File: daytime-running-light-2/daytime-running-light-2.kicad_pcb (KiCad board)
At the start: 2 copper layers, 163.2 x 88.6 mm, 58 parts, among them J1 Conn_01x01_Socket, J2 Conn_01x01_Socket, J3 Conn_01x01_Socket, J4 Conn_01x01_Socket, J5 Conn_01x01_Socket, J6 Conn_01x01_Pin, J7 Conn_01x01_Socket, J8 Conn_01x01_Socket, J9 Conn_01x01_Socket, Q1 BC548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

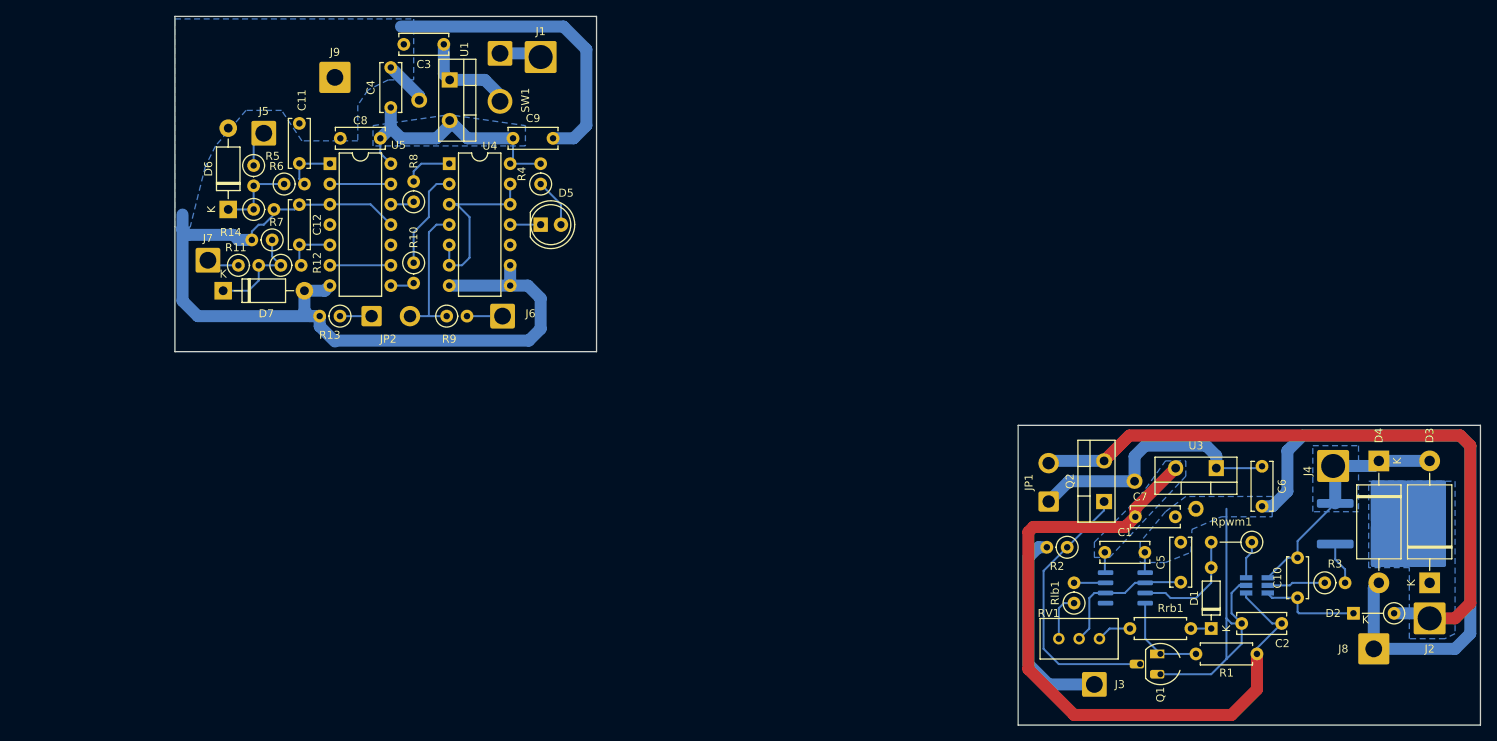
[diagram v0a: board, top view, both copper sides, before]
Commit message: [DRL] [soft-start] Update track widths. Prepare for plotting
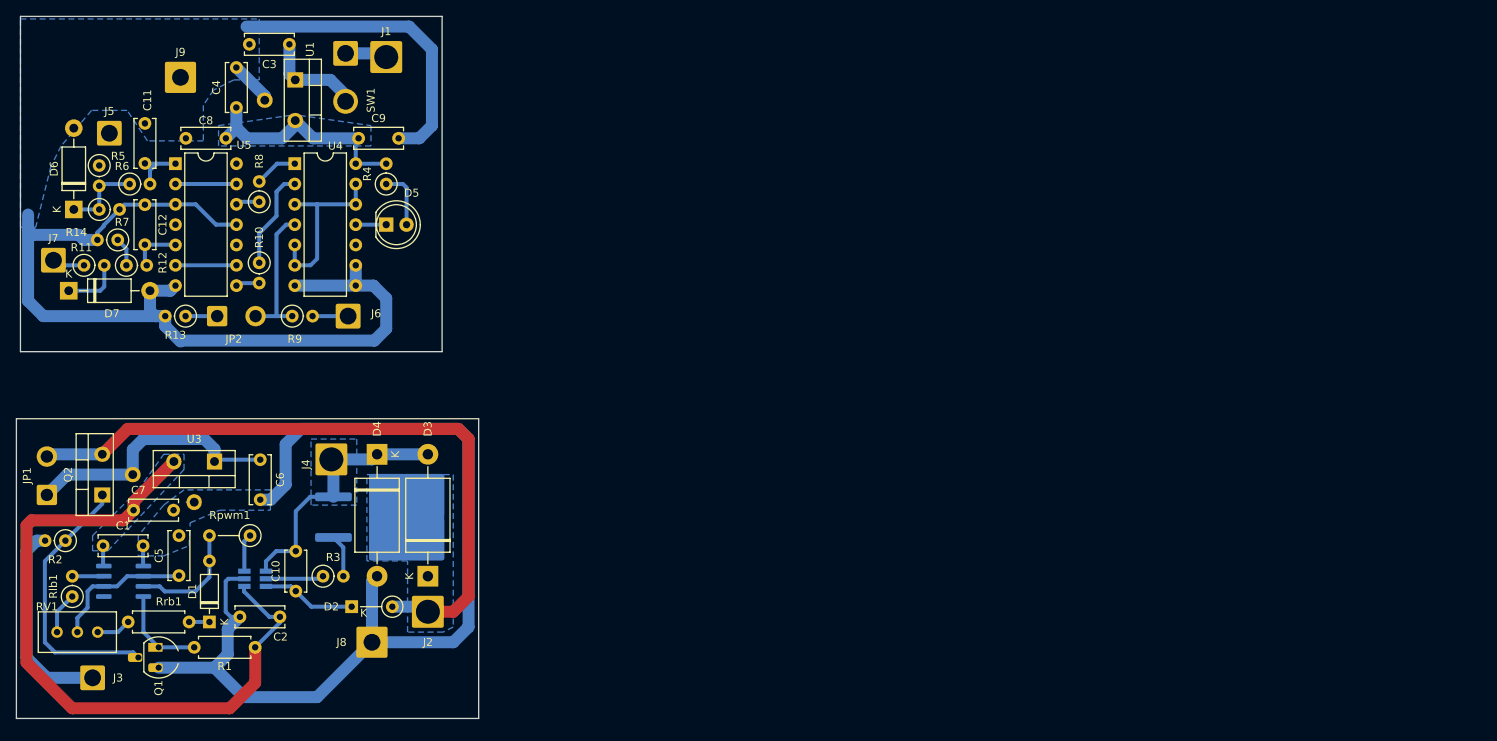
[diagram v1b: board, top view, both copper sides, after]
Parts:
- moved C1 125.2 mm to (30.4, 84.9)
- moved C10 125.2 mm to (54.5, 90.6)
- moved C2 125.2 mm to (52.5, 93.8)
- moved C7 125.2 mm to (34.2, 80.5)
- moved D3 125.2 mm to (71.0, 88.7)
- moved D4 125.2 mm to (64.6, 73.5)
- moved J2 125.2 mm to (71.0, 93.2)
- moved J3 125.2 mm to (29.1, 101.4)
- moved J4 125.2 mm to (58.9, 74.1)
- moved JP1 125.2 mm to (23.4, 78.5)
- moved Q1 125.2 mm to (37.3, 97.6)
- moved Q2 125.2 mm to (30.3, 78.5)
- moved Q3 125.2 mm to (66.8, 81.3)
- moved R1 125.2 mm to (49.4, 97.6)
- moved Rpwm1 125.2 mm to (48.8, 83.6)
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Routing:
- net GND2: track 123.8 -> 129.0 mm
- net /VCC_STAB: track 33.2 -> 30.0 mm
- net Net-(C11-Pad1): track 6.68 -> 9.56 mm
- net /HEADLIGHT: track 4.56 -> 1.80 mm
- net /POWER_OUTPUT: track 33.3 -> 35.7 mm
- net Net-(D7-K): track 13.3 -> 10.9 mm
- net Net-(D5-A): track 6.13 -> 7.36 mm
- net Net-(D2-K): track 12.9 -> 11.8 mm
- net Net-(R8-Pad2): track 6.11 -> 5.37 mm
- net Net-(RV1-Pad3): track 5.98 -> 5.23 mm
- net /ALLOW_POWER_ON: track 34.4 -> 33.9 mm
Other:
- board size 163.2 x 88.6 mm -> 57.8 x 87.8 mm
